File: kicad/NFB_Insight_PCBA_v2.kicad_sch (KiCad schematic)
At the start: 0 parts

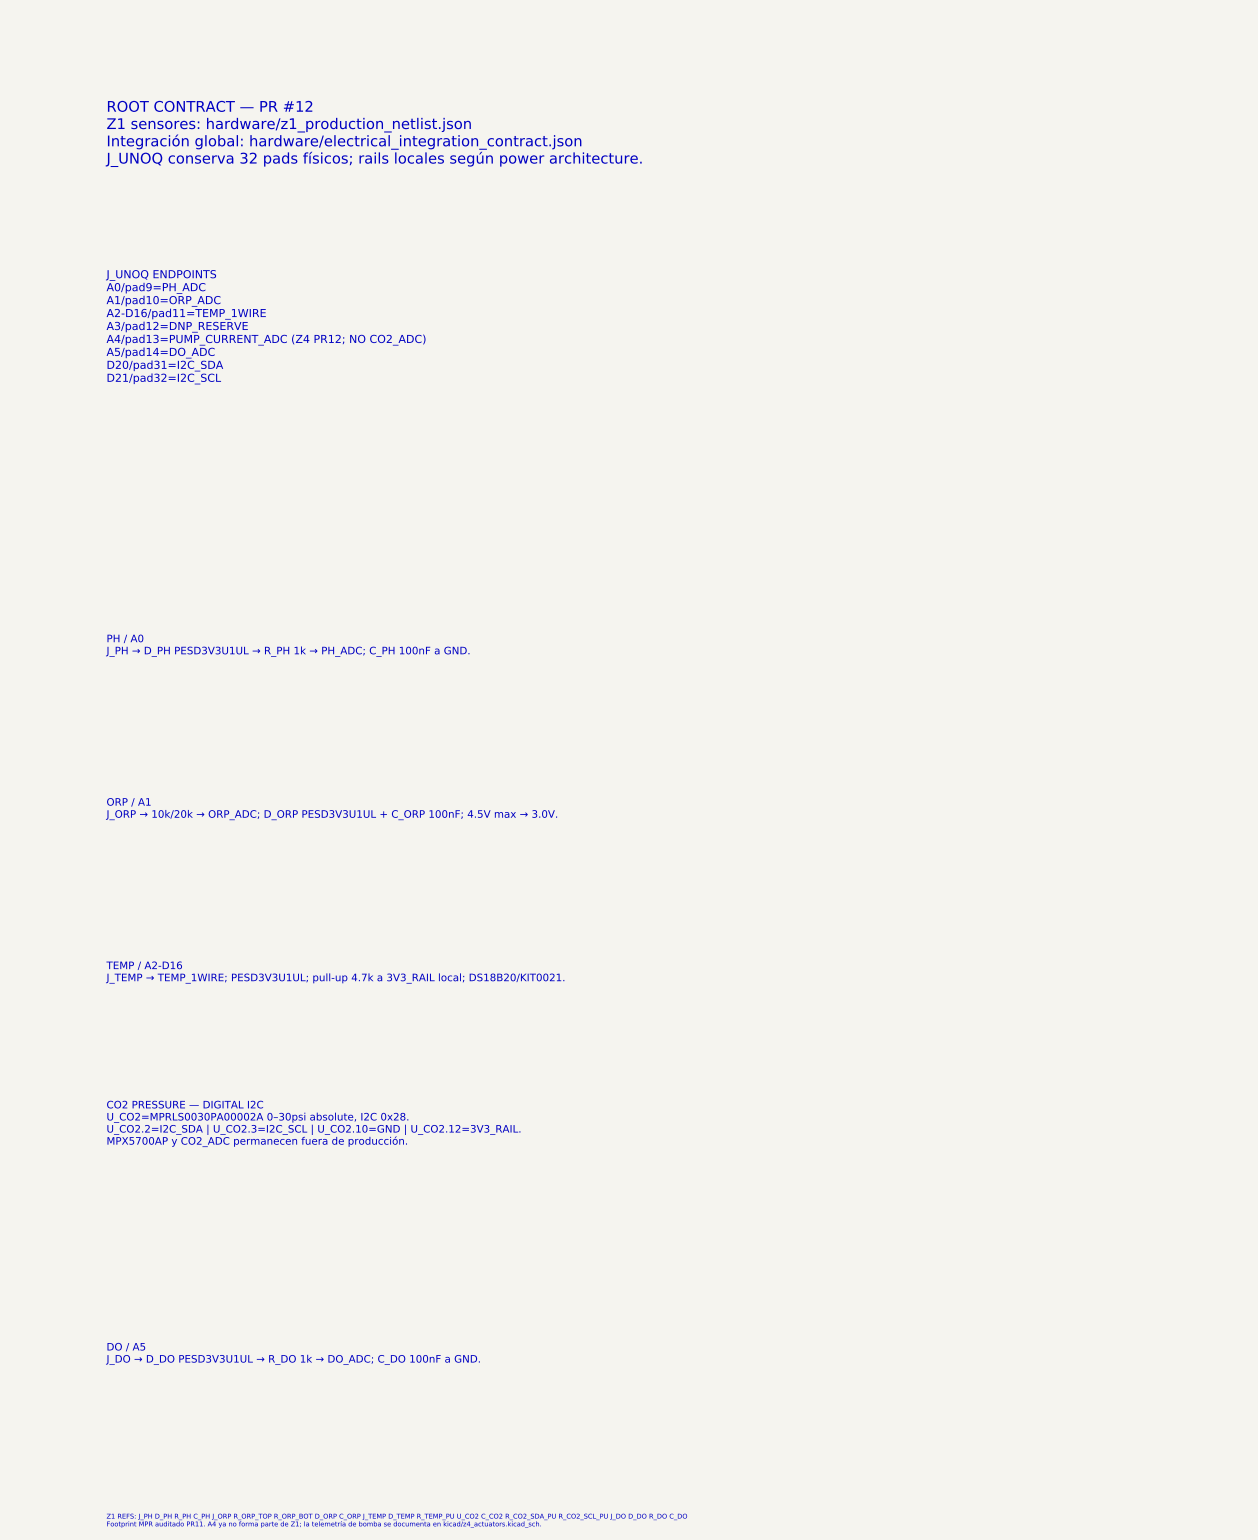
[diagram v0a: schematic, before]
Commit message: eda: reemplazar root contractual por jerarquía inter-zona PR14
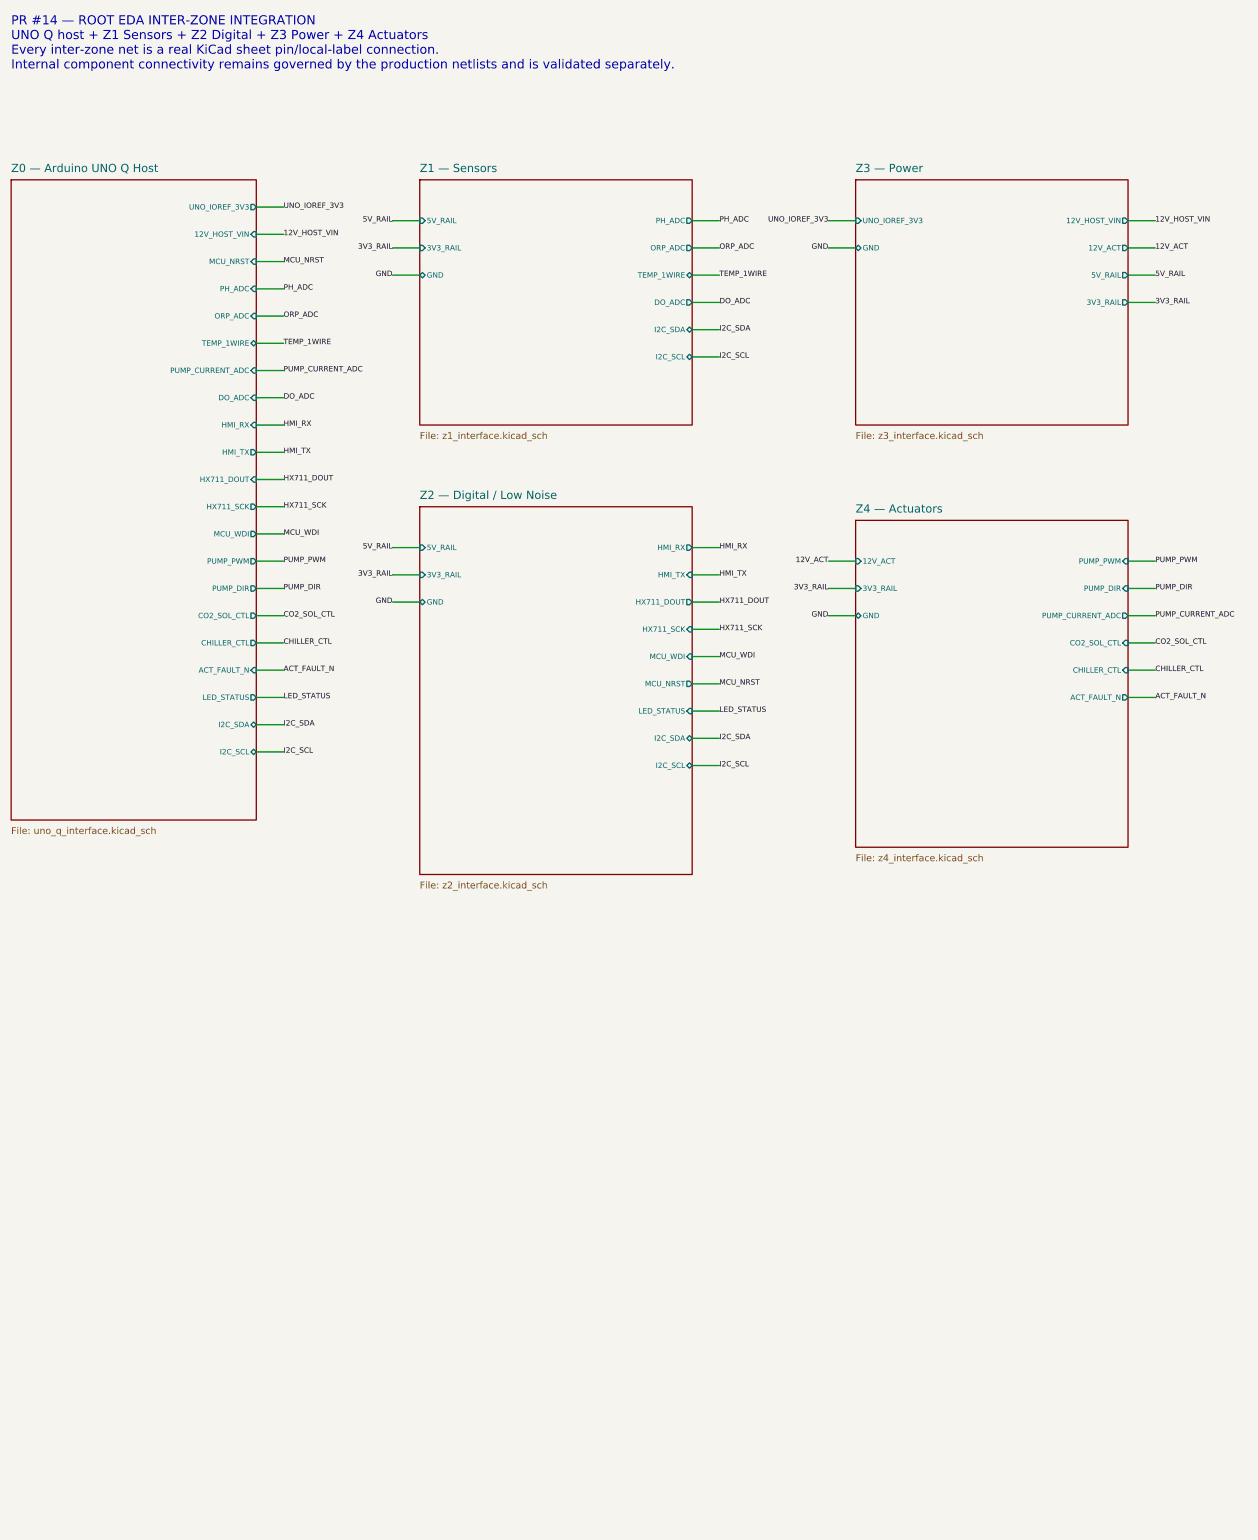
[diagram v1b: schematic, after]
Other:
- added sheet Z0 — Arduino UNO Q Host (uno_q_interface.kicad_sch)
- added sheet Z1 — Sensors (z1_interface.kicad_sch)
- added sheet Z2 — Digital / Low Noise (z2_interface.kicad_sch)
- added sheet Z3 — Power (z3_interface.kicad_sch)
- added sheet Z4 — Actuators (z4_interface.kicad_sch)
- note added: "PR #14 — ROOT EDA INTER-ZONE INTEGRATION UNO Q host + Z1 Sensors + Z2 Digital + Z3 Power + Z4 Actuators Every inter-zone net is a real KiCad sheet pin/local-label connection. Internal component connectivity remains governed by the production netlists and is validated separately."
- note removed: "CO2 PRESSURE — DIGITAL I2C U_CO2=MPRLS0030PA00002A 0–30psi absolute, I2C 0x28. U_CO2.2=I2C_SDA | U_CO2.3=I2C_SCL | U_CO2.10=GND | U_CO2.12=3V3_RAIL. MPX5700AP y CO2_ADC permanecen fuera de producción."
- note removed: "DO / A5 J_DO → D_DO PESD3V3U1UL → R_DO 1k → DO_ADC; C_DO 100nF a GND."
- note removed: "J_UNOQ ENDPOINTS A0/pad9=PH_ADC A1/pad10=ORP_ADC A2-D16/pad11=TEMP_1WIRE A3/pad12=DNP_RESERVE A4/pad13=PUMP_CURRENT_ADC (Z4 PR12; NO CO2_ADC) A5/pad14=DO_ADC D20/pad31=I2C_SDA D21/pad32=I2C_SCL"
- note removed: "ORP / A1 J_ORP → 10k/20k → ORP_ADC; D_ORP PESD3V3U1UL + C_ORP 100nF; 4.5V max → 3.0V."
- note removed: "PH / A0 J_PH → D_PH PESD3V3U1UL → R_PH 1k → PH_ADC; C_PH 100nF a GND."
- note removed: "ROOT CONTRACT — PR #12 Z1 sensores: hardware/z1_production_netlist.json Integración global: hardware/electrical_integration_contract.json J_UNOQ conserva 32 pads físicos; rails locales según power architecture."
- note removed: "TEMP / A2-D16 J_TEMP → TEMP_1WIRE; PESD3V3U1UL; pull-up 4.7k a 3V3_RAIL local; DS18B20/KIT0021."
- note removed: "Z1 REFS: J_PH D_PH R_PH C_PH J_ORP R_ORP_TOP R_ORP_BOT D_ORP C_ORP J_TEMP D_TEMP R_TEMP_PU U_CO2 C_CO2 R_CO2_SDA_PU R_CO2_SCL_PU J_DO D_DO R_DO C_DO Footprint MPR auditado PR11. A4 ya no forma parte de Z1; la telemetría de bomba se documenta en kicad/z4_actuators.kicad_sch."
- title: NFB Insight PCBA v2 — Root Contract / Z1 Sensors -> NFB Insight PCBA v2 — Root EDA Inter-Zone Hierarchy

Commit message: eda: cerrar GND común y compactar root jerárquico PR14
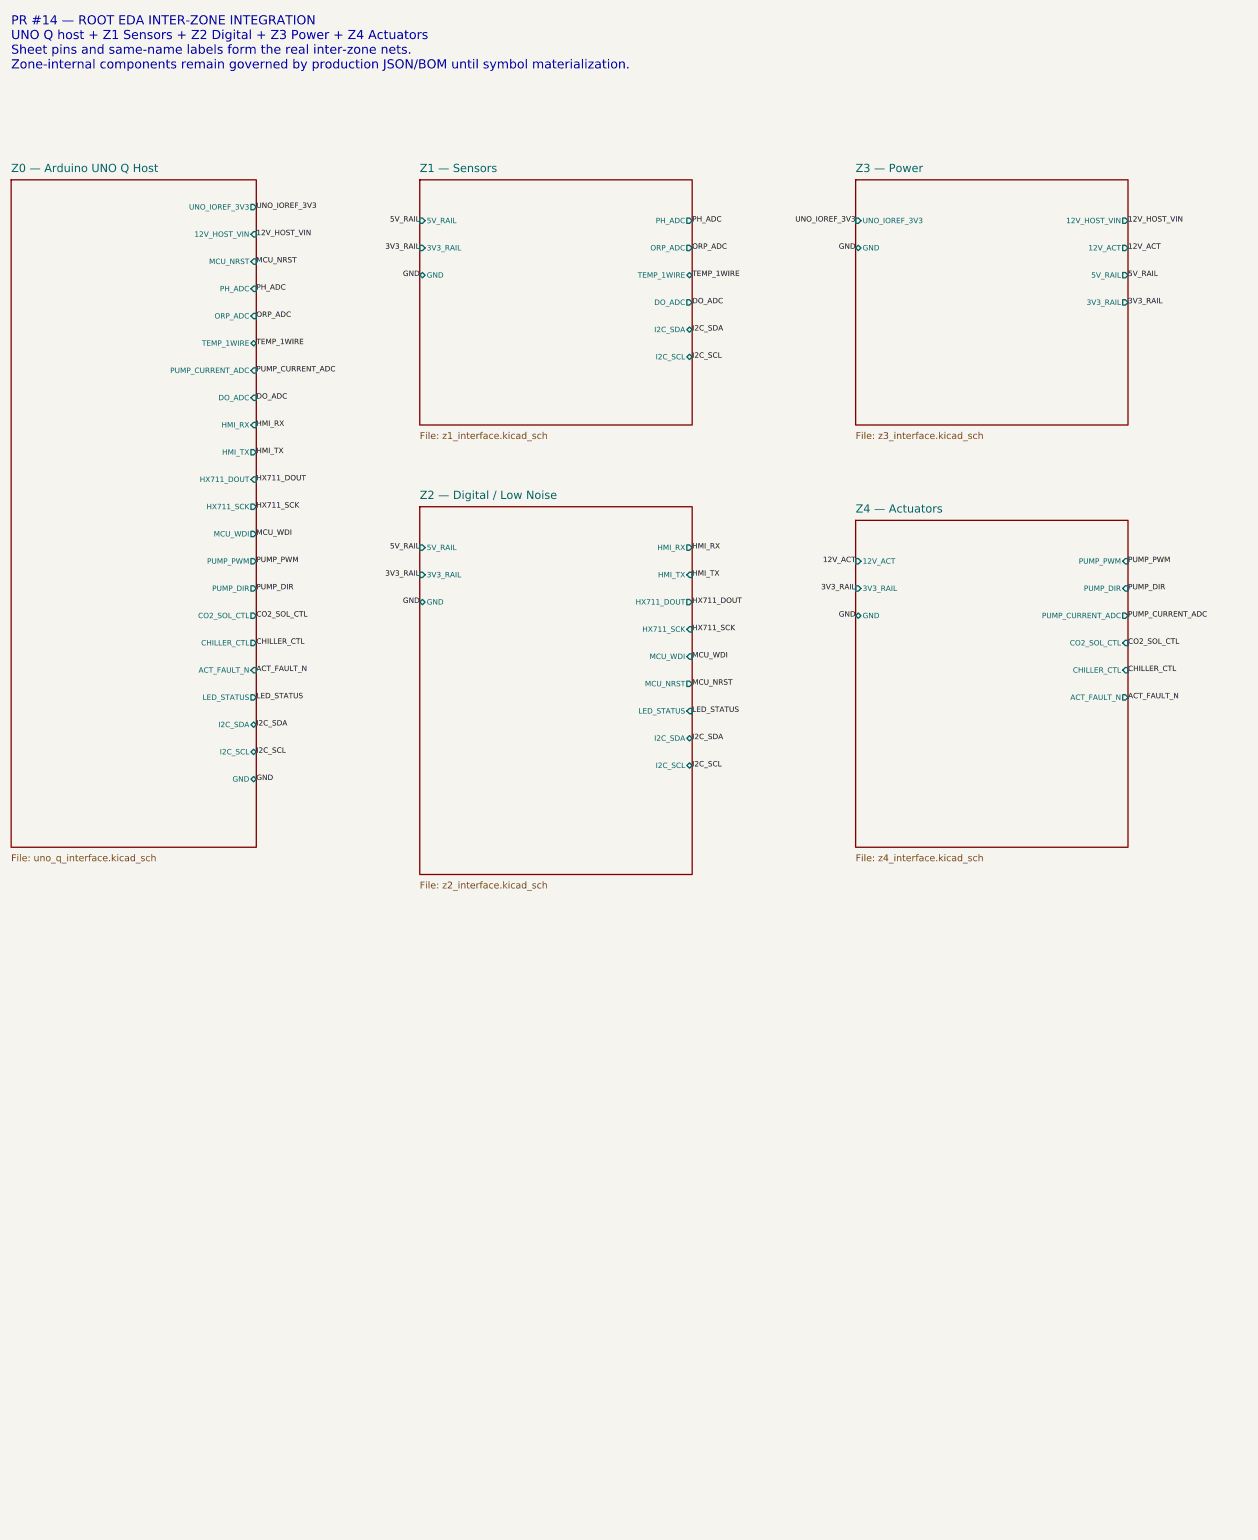
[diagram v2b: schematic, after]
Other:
- sheet Z0 — Arduino UNO Q Host ports: added GND; removed none
- note added: "PR #14 — ROOT EDA INTER-ZONE INTEGRATION UNO Q host + Z1 Sensors + Z2 Digital + Z3 Power + Z4 Actuators Sheet pins and same-name labels form the real inter-zone nets. Zone-internal components remain governed by production JSON/BOM until symbol materialization."
- note removed: "PR #14 — ROOT EDA INTER-ZONE INTEGRATION UNO Q host + Z1 Sensors + Z2 Digital + Z3 Power + Z4 Actuators Every inter-zone net is a real KiCad sheet pin/local-label connection. Internal component connectivity remains governed by the production netlists and is validated separately."
